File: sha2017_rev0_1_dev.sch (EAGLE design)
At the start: 82 parts, among them IC1 CP210X_USB_UART, IC2 AP7215, IC32 ESP32_AI, Q1 MMBT2222A, Q2 MMBT2222A, Q6 MOSFET-NCHANNELBSS123LT1G, SW801 MCMT5-F-V, X701 2908-05WB-MG

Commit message: fixed all part designators
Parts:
- removed C26: 4u7/16V, rcl:C-EUC0805
- removed C27: 2u2/16V, rcl:C-EUC0805
- removed D10, D11: NSVR0320MW2T1G, SparkFun-DiscreteSemi:BAT20JFILM
- removed SJ14: JUMPER-PAD-2-NC_BY_TRACE, SparkFun-Passives:JUMPER-PAD-2-NC_BY_TRACE
- added C8: 100n, rcl:C-EUC0805
- added C9: 1u, rcl:C-EUC0603
- added D100, D6: (no value), SparkFun-LED:LED0603
- added SJ1: JUMPER-PAD-2-NC_BY_TRACE, SparkFun-Passives:JUMPER-PAD-2-NC_BY_TRACE
- C1: value 100n -> 4u7/16V; device rcl:C-EUC0603 -> 00ralf:C0603-DASHES
- C10, C13: value 4u7/16V -> 1u; device 00ralf:C0603-DASHES -> rcl:C-EUC0603
- C11: device rcl:C-EUC0805 -> rcl:C-EUC0603
- C12: value 4u7/16V -> 1u; device rcl:C-EUC0805 -> rcl:C-EUC0603
- C14, C7: value 100n -> 1u
- C15: value 4u7/16V -> 100n; device rcl:C-EUC0805 -> rcl:C-EUC0603
- C19: device rcl:C-EUC0603 -> 00ralf:C0603-DASHES
- C2: value 100n -> 2u2/16V; device rcl:C-EUC0603 -> rcl:C-EUC0805
- C20: value 1u -> 100n
- C21, C22: value 1u -> 4u7/16V; device rcl:C-EUC0603 -> rcl:C-EUC0805
- C23, C24: value 1u -> (none); OC_FARNELL (none) -> unknown
- C25: value 1u -> 100n; device 00ralf:C0603-DASHES -> rcl:C-EUC0603
- C3: value (none) -> 100n; device rcl:C-EUC0603 -> rcl:C-EUC0805; OC_FARNELL unknown -> (none)
- C4: value (none) -> 4u7/16V; device rcl:C-EUC0603 -> rcl:C-EUC0805; OC_FARNELL unknown -> (none)
- C5: value 100n -> 4u7/16V; device rcl:C-EUC0805 -> 00ralf:C0603-DASHES
- D1: value (none) -> PMEG4005EJ; device SparkFun-LED:LED0603 -> SparkFun-DiscreteSemi:DIODE-SCHOTTKY-PMEG4005EJ
- D2: value (none) -> NSVR0320MW2T1G; device SparkFun-LED:LED0603 -> SparkFun-DiscreteSemi:BAT20JFILM
- D3: value PMEG4005EJ -> NSVR0320MW2T1G; device SparkFun-DiscreteSemi:DIODE-SCHOTTKY-PMEG4005EJ -> SparkFun-DiscreteSemi:BAT20JFILM
- IC1: value CP210X_USB_UART -> AP7215; device SparkFun-DigitalIC:CP210X_USB_UART -> badge:AP7215
- IC2: value AP7215 -> (none); device badge:AP7215 -> SparkFun-PowerIC:V_REG_LM1117SOT223
- IC3: value (none) -> CP210X_USB_UART; device SparkFun-PowerIC:V_REG_LM1117SOT223 -> SparkFun-DigitalIC:CP210X_USB_UART
- JP2: value M11LOCK -> M09LOCK; device SparkFun-Connectors:M11LOCK -> SparkFun-Connectors:M09LOCK
- JP3: value M09LOCK -> M11LOCK; device SparkFun-Connectors:M09LOCK -> SparkFun-Connectors:M11LOCK
- R1, R2: value 10K -> (none)
- R11: value 10k -> (none)
- R14, R15, R16, R17: value (none) -> 10k
- R4: value 10k -> (none); OC_FARNELL unknown -> (none)
- R5, R6: value 10k -> 10K
- R7: value 10k -> 5R; device rcl:R-EU_R0603 -> 00ralf:R0603-DASHES
- R8: OC_FARNELL (none) -> unknown
- R9: value 5R -> 10k; device 00ralf:R0603-DASHES -> rcl:R-EU_R0603
- renumbered IC32 to IC4, J2 to J1, Q6 to Q3, R714 to R10, S5 to S101, S6 to S100, SW801 to SW100, USB100 to USB1
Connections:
- net +3V3: now also C19.1, C20.1, C21.1, C22.1, C4.1, C5.1, IC1.OUT, IC2.OUT@1, JP1.11, R15.2, R16.2, R17.2, R8.1, R9.2; no longer C12.1, C13.1, C14.1, C26.1, C6.1, C7.1, IC3.OUT, IC3.OUT@1, JP2.11, R4.1, R5.2, R6.2, R7.2, R8.2
- net +5V: now also C2.1, C3.1, C8.1, D1.C, IC1.IN, IC3.REGIN, IC3.VBUS; no longer C10.1, C27.1, C5.1, D3.C, IC1.REGIN, IC1.VBUS, IC3.IN
- net BT_B: now also R17.1, SJ13.1; no longer R12.1, SJ7.1
- net BT_DOWN: now also R13.1, SJ9.1; no longer R6.1, SJ3.1
- net BT_LEFT: now also R14.1, SJ10.1; no longer R7.1, SJ4.1
- net BT_MID: now also R15.1, SJ11.1; no longer R11.1, SJ6.1
- net BT_RIGHT: now also R12.1, SJ8.1; no longer R8.1, SJ2.1
- net BT_UP: now also R16.1, SJ12.1; no longer R5.1, SJ5.1
- net ESP32_!RESET: now also JP3.10, R8.2; no longer JP1.10, R4.2
- net ESP32_FLASH/TOUCHE_MENU: now also JP2.3, R9.1; no longer JP3.3, R13.1
- net ESP32_RX: now also D4.C, IC3.TXD, JP1.4; no longer D2.C, IC1.TXD, JP2.4
- net ESP32_TX: now also D6.C, IC3.RXD, JP1.3; no longer D4.C, IC1.RXD, JP2.3
- net GND: now also C10.1, C12.1, C13.1, C19.2, C20.2, C21.2, C22.2, C3.2, C4.2, C7.1, C8.2, C9.1, D1.A, D3.C, IC2.ADJ, IC3.GND, IC3.GND@EXP, IC3.GND@M, JP1.1, JP2.5, JP3.11, R7.2; no longer C10.2, C12.2, C13.2, C14.2, C20.1, C21.1, C22.1, C26.2, C27.2, C3.1, C4.1, C7.2, D11.C, D3.A, IC1.GND@EXP, IC1.GND@M, IC2.GND, IC3.ADJ, JP1.11, JP2.1, JP3.5, R9.2
- net LCD_!RESET: now also SJ3.2; no longer SJ8.2
- net LCD_BUSY: now also SJ2.2; no longer SJ12.2
- net LCD_CS: now also SJ5.2; no longer SJ9.2
- net LCD_D/!S: now also SJ4.2; no longer SJ14.2
- net LCD_MOSI: now also SJ7.2; no longer SJ11.2
- net LCD_SCK: now also SJ6.2; no longer SJ10.2
- net LED1: now also D100.C, SJ1.2; no longer D1.C, SJ13.2
- net N$1: now also C23.2, JP3.9; no longer C3.2, JP1.9
- net N$10: now also IC3.RTS, R5.1; no longer IC1.RTS, R2.1
- net N$11: now also IC3.DTR, R6.1; no longer IC1.DTR, R1.1
- net N$12: now also JP3.6, SJ8.2; no longer JP1.6, SJ2.2
- net N$13: now also R5.2; no longer R2.2
- net N$14: now also R6.2; no longer R1.2
- net N$15: now also JP3.7; no longer JP1.7
- net N$16: now also JP1.2, SJ1.1; no longer JP2.2, SJ13.1
- net N$17: now also JP1.5, SJ2.1; no longer JP2.5, SJ12.1
- net N$18: now also JP1.7, SJ4.1; no longer JP2.7, SJ14.1
- net N$19: now also JP1.6, SJ3.1; no longer JP2.6, SJ8.1
- net N$2: now also C24.2, JP3.8; no longer C4.2, JP1.8
- net N$20: now also JP1.8, SJ5.1; no longer JP2.8, SJ9.1
- net N$21: now also JP1.9, SJ6.1; no longer JP2.9, SJ10.1
- net N$22: now also C14.1, D2.C, D3.A; no longer C19.1, D10.C, D11.A
- net N$23: now also C14.2; no longer C19.2
- net N$24: now also JP1.10, SJ7.1; no longer JP2.10, SJ11.1
- net N$25: now also D100.A, R11.1; no longer D1.A, R14.1
- net N$26: now also R2.1; no longer R15.1
- net N$27: now also D4.A, R1.1; no longer D2.A, R16.1
- net N$28: now also D6.A, R4.1; no longer D4.A, R17.1
- net N$3: now also JP3.1, SJ13.2; no longer JP1.1, SJ7.2
- net N$4: now also JP3.2, SJ12.2; no longer JP1.2, SJ5.2
- net N$6: now also JP3.3, SJ11.2; no longer JP1.3, SJ6.2
- net N$7: now also JP3.4, SJ10.2; no longer JP1.4, SJ4.2
- net N$8: now also IC3.!RST; no longer IC1.!RST
- net N$9: now also JP3.5, SJ9.2; no longer JP1.5, SJ3.2
- net PREVGH: now also C13.2; no longer C17.2
- net PREVGL: now also C9.2, D2.A; no longer C18.2, D10.A
- net RESE: now also R7.1; no longer R9.1
- net SD_CD: now also JP2.1; no longer JP3.1
- net SD_CLK: now also JP2.9; no longer JP3.9
- net SD_CMD: now also JP2.6; no longer JP3.6
- net SD_DATA0: now also JP2.4; no longer JP3.4
- net SD_DATA1: now also JP2.2; no longer JP3.2
- net SD_DATA2: now also JP2.8; no longer JP3.8
- net SD_DATA3: now also JP2.7; no longer JP3.7
- net USB_DN_CON: now also IC3.D-; no longer IC1.D-
- net USB_DP_CON: now also IC3.D+; no longer IC1.D+
- net VCOM: now also C7.2; no longer C24.2
- net VDD: now also C6.1, IC3.VDD, R1.2, R2.2, R4.2; no longer C2.1, IC1.VDD, R15.2, R16.2, R17.2
- net VGH: now also C17.2; no longer C21.2
- net VGL: now also C18.2; no longer C20.2
- net VSH: now also C12.2; no longer C22.2
- net VSL: now also C10.2; no longer C23.2

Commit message: some PCB tweeking
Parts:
- added FD1, FD2, FD3, FD4, FD5: FIDUCIAL, adafruit:FIDUCIAL
- D1: value PMEG4005EJ -> SD05-7
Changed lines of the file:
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@@
 <part name="GND46" library="supply1" deviceset="GND" device=""/>
 <part name="F1" library="SparkFun-PowerIC" deviceset="PTC" device="SMD" value="500mA"/>
-<part name="D1" library="SparkFun-DiscreteSemi" deviceset="DIODE-SCHOTTKY" device="-PMEG4005EJ" value="PMEG4005EJ"/>
+<part name="D1" library="SparkFun-DiscreteSemi" deviceset="DIODE-SCHOTTKY" device="-PMEG4005EJ" value="SD05-7"/>
 <part name="GND26" library="supply1" deviceset="GND" device=""/>
 <part name="FRAME1" library="frames" deviceset="A3L-LOC" device=""/>
@@
 <part name="C15" library="rcl" deviceset="C-EU" device="C0603" value="100n"/>
 <part name="GND17" library="supply1" deviceset="GND" device=""/>
+<part name="FD4" library="adafruit" deviceset="FIDUCIAL" device="">
+<attribute name="MF" value=""/>
+<attribute name="MPN" value=""/>
+<attribute name="OC_FARNELL" value="unknown"/>
+</part>
+<part name="FD3" library="adafruit" deviceset="FIDUCIAL" device="">
+<attribute name="MF" value=""/>
+<attribute name="MPN" value=""/>
+<attribute name="OC_FARNELL" value="unknown"/>
+</part>
+<part name="FD1" library="adafruit" deviceset="FIDUCIAL" device="">
+<attribute name="MF" value=""/>
+<attribute name="MPN" value=""/>
+<attribute name="OC_FARNELL" value="unknown"/>
+</part>
+<part name="FD2" library="adafruit" deviceset="FIDUCIAL" device="">
+<attribute name="MF" value=""/>
+<attribute name="MPN" value=""/>
+<attribute name="OC_FARNELL" value="unknown"/>
+</part>
+<part name="FD5" library="adafruit" deviceset="FIDUCIAL" device="">
+<attribute name="MF" value=""/>
+<attribute name="MPN" value=""/>
+<attribute name="OC_FARNELL" value="unknown"/>
+</part>
 </parts>
 <sheets>
@@
 <instance part="C15" gate="G$1" x="165.1" y="71.12"/>
 <instance part="GND17" gate="1" x="165.1" y="63.5"/>
+<instance part="FD4" gate="G$1" x="16.51" y="10.16">
+<attribute name="OC_FARNELL" x="16.51" y="10.16" size="1.778" layer="96" rot="MR0" display="off"/>
+<attribute name="MF" x="16.51" y="10.16" size="1.778" layer="96" rot="MR0" display="off"/>
+<attribute name="MPN" x="16.51" y="10.16" size="1.778" layer="96" rot="MR0" display="off"/>
+</instance>
+<instance part="FD3" gate="G$1" x="25.4" y="10.16">
+<attribute name="OC_FARNELL" x="25.4" y="10.16" size="1.778" layer="96" rot="MR0" display="off"/>
+<attribute name="MF" x="25.4" y="10.16" size="1.778" layer="96" rot="MR0" display="off"/>
+<attribute name="MPN" x="25.4" y="10.16" size="1.778" layer="96" rot="MR0" display="off"/>
+</instance>
+<instance part="FD1" gate="G$1" x="34.29" y="10.16">
+<attribute name="OC_FARNELL" x="34.29" y="10.16" size="1.778" layer="96" rot="MR0" display="off"/>
+<attribute name="MF" x="34.29" y="10.16" size="1.778" layer="96" rot="MR0" display="off"/>
+<attribute name="MPN" x="34.29" y="10.16" size="1.778" layer="96" rot="MR0" display="off"/>
+</instance>
+<instance part="FD2" gate="G$1" x="43.18" y="10.16">
+<attribute name="OC_FARNELL" x="43.18" y="10.16" size="1.778" layer="96" rot="MR0" display="off"/>
+<attribute name="MF" x="43.18" y="10.16" size="1.778" layer="96" rot="MR0" display="off"/>
+<attribute name="MPN" x="43.18" y="10.16" size="1.778" layer="96" rot="MR0" display="off"/>
+</instance>
+<instance part="FD5" gate="G$1" x="50.8" y="10.16">
+<attribute name="OC_FARNELL" x="50.8" y="10.16" size="1.778" layer="96" rot="MR0" display="off"/>
+<attribute name="MF" x="50.8" y="10.16" size="1.778" layer="96" rot="MR0" display="off"/>
+<attribute name="MPN" x="50.8" y="10.16" size="1.778" layer="96" rot="MR0" display="off"/>
+</instance>
 </instances>
 <busses>

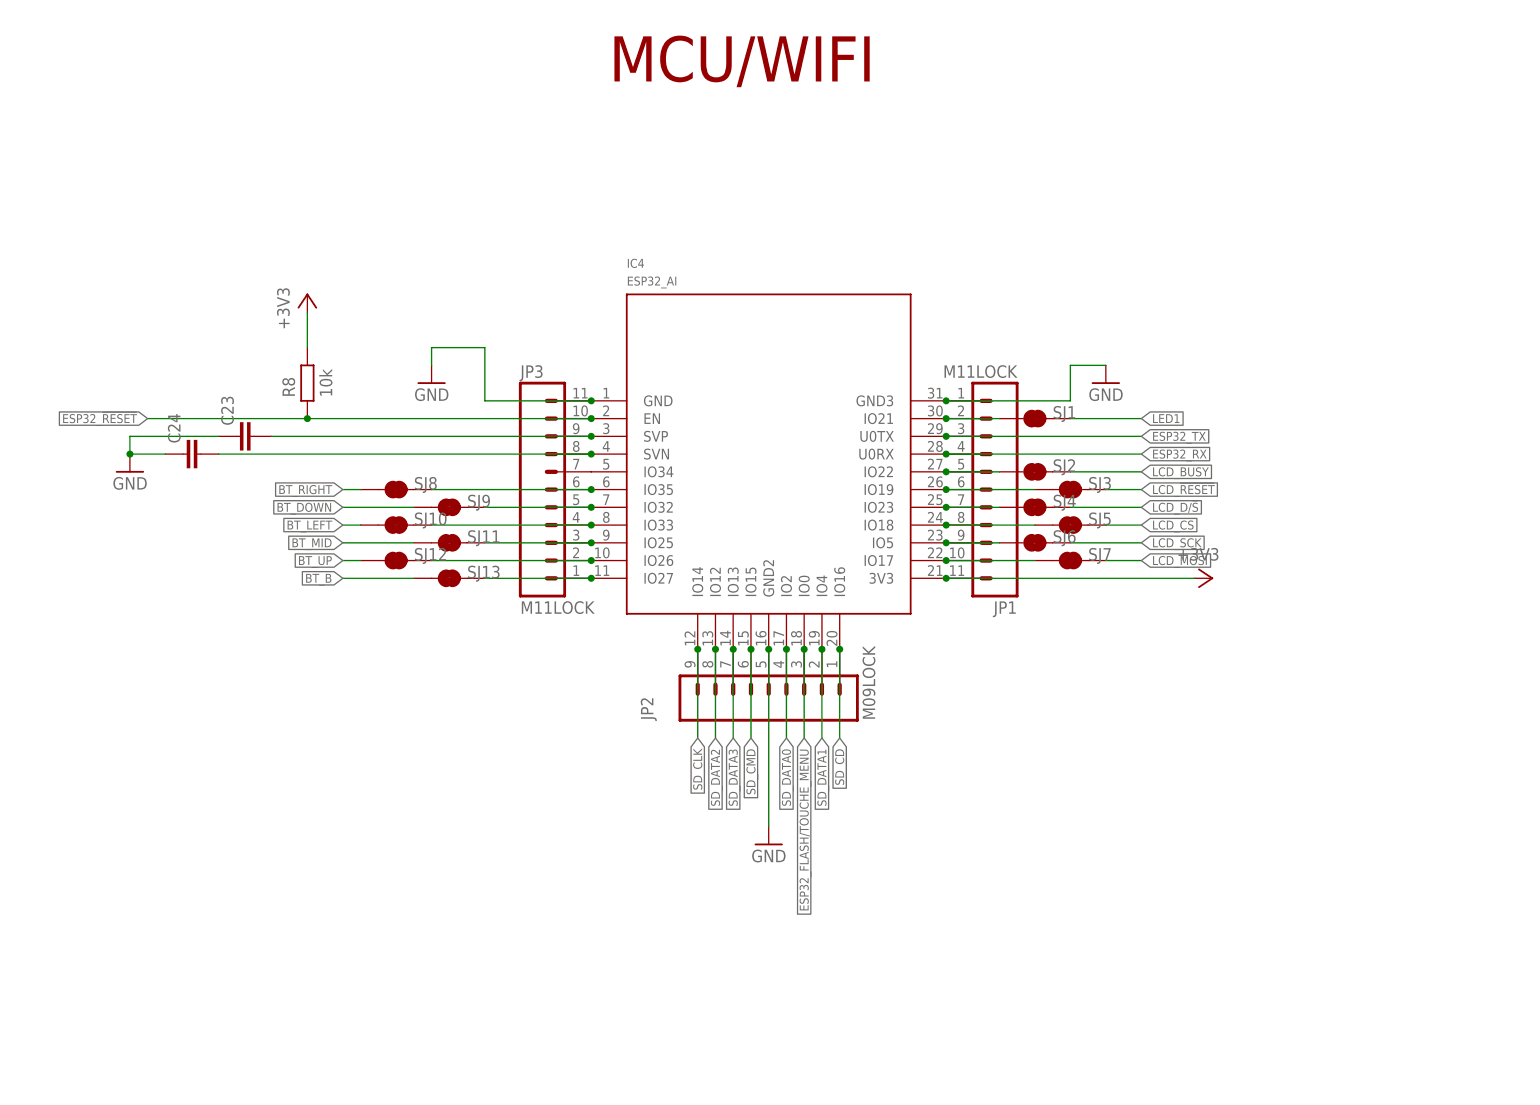
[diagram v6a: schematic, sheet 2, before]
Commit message: changed ESP module to WROOM32
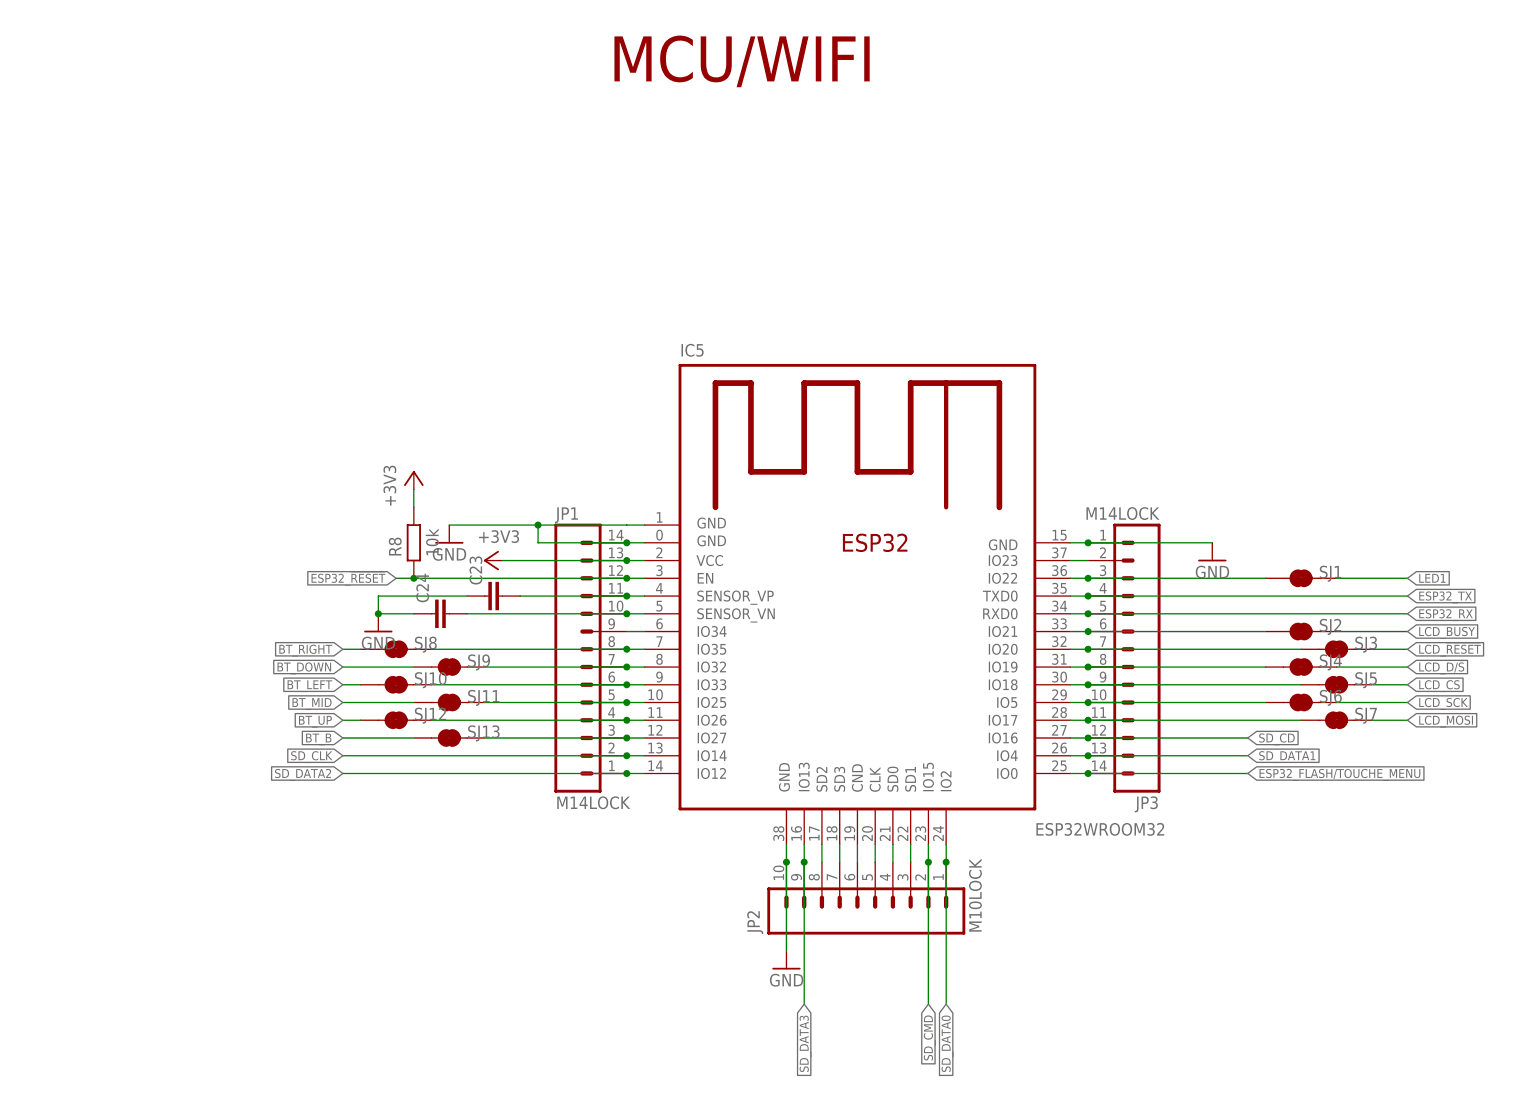
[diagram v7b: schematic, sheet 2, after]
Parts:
- removed IC4: ESP32_AI, badge:ESP32_AI
- added IC5: ESP32WROOM32, ESP3x:ESP32WROOM32
- C1, C5: value 4u7/16V -> 100n; device 00ralf:C0603-DASHES -> rcl:C-EUC0603; PARTNO (none) -> GRM188R71H104KA93D
- C10, C12, C13, C14, C17, C18, C7, C9: PARTNO (none) -> GRM188R61E105KA12D
- C11, C15, C20, C25, C6: PARTNO (none) -> GRM188R71H104KA93D
- C16, C21, C22, C4: PARTNO (none) -> GRM21BR61C475KA88K
- C19: device 00ralf:C0603-DASHES -> rcl:C-EUC0603; PARTNO (none) -> GRM188R61E105KA12D
- C2: value 2u2/16V -> 4u7/16V; PARTNO (none) -> GRM21BR61C475KA88K
- C3, C8: value 100n -> 4u7/16V; PARTNO (none) -> GRM21BR61C475KA88K
- D1: PARTNO (none) -> PMEG4005EJ,115
- D100: value (none) -> Green; device SparkFun-LED:LED0603 -> led:LEDSML1206; PARTNO (none) -> 156120VS75300
- D2, D3, D7: PARTNO (none) -> BAT20JFILM
- D4: value (none) -> Yellow
- D5: value (none) -> green
- D6: value (none) -> RED
- F1: PARTNO (none) -> 0ZCJ0025FF2E
- IC1: PARTNO (none) -> AP7215-33YG-13
- IC2: value (none) -> LM1117; PARTNO (none) -> LM1117MPX-3.3/NOPB
- IC3: PARTNO (none) -> CP2102-GMR
- J1: PARTNO (none) -> 68712414022
- JP1, JP3: value M11LOCK -> M14LOCK; device SparkFun-Connectors:M11LOCK -> SparkFun-Connectors:M14LOCK
- JP2: value M09LOCK -> M10LOCK; device SparkFun-Connectors:M09LOCK -> SparkFun-Connectors:M10LOCK
- L1: PARTNO (none) -> NLCV32T-220K-EF
- Q1, Q2: PARTNO (none) -> BC817-25,215
- Q3: value MOSFET-NCHANNELBSS123LT1G -> SI1304 BDL; device SparkFun-DiscreteSemi:MOSFET-NCHANNELBSS123LT1G -> SparkFun-DiscreteSemi:MOSFET-NCHANNEL2N7002PW; PARTNO (none) -> SI1308EDL-T1-GE3
- R1, R11, R2, R4: value (none) -> 1k; PARTNO (none) -> ERJ-3GEYJ102V
- R10: PARTNO (none) -> CRCW0603100KFKEA
- R12, R13, R14, R15, R16, R17, R8, R9: PARTNO (none) -> ERJ-3GEYJ103V
- R3: device 00ralf:R0603-DASHES -> rcl:R-EU_R0603; PARTNO (none) -> ERJ-3GEYJ103V
- R5, R6: value 10K -> 10k; PARTNO (none) -> ERJ-3GEYJ103V
- R7: PARTNO (none) -> ERJ-3GEYJ5R1V
- S1, S100, S101: PARTNO (none) -> SKHMQME010
- SW100: PARTNO (none) -> SKRHAAE010
- USB1: PARTNO (none) -> 10118194-0001LF
- X701: PARTNO (none) -> 2908-05WB-MG
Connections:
- removed net N$19: IC4.IO19, JP1.6, SJ3.1
- removed net N$2: C24.2, IC4.SVN, JP3.8
- new net N$42: C23.2, IC5.SENSOR_VP, JP1.11
- new net N$43: C24.2, IC5.SENSOR_VN, JP1.10
- new net N$44: IC5.IO35, JP1.8, SJ8.2
- new net N$45: IC5.IO32, JP1.7, SJ9.2
- new net N$46: IC5.IO33, JP1.6, SJ10.2
- new net N$47: IC5.IO25, JP1.5, SJ11.2
- new net N$48: IC5.IO26, JP1.4, SJ12.2
- new net N$49: IC5.IO27, JP1.3, SJ13.2
- new net N$63: IC5.IO19, JP3.8, SJ4.1
- net +3V3: now also IC5.VCC, JP1.13; no longer IC4.3V3, JP1.11
- net ESP32_!RESET: now also IC5.EN, JP1.12; no longer IC4.EN, JP3.10
- net ESP32_FLASH/TOUCHE_MENU: now also IC5.IO0, JP3.14; no longer IC4.IO0, JP2.3
- net ESP32_RX: now also IC5.RXD0, JP3.5; no longer IC4.U0RX, JP1.4
- net ESP32_TX: now also IC5.TXD0, JP3.4; no longer IC4.U0TX, JP1.3
- net GND: now also IC5.GND, IC5.GND@0, IC5.GND@1, IC5.GND@3, JP1.14, JP2.10, JP3.1; no longer IC4.GND, IC4.GND2, IC4.GND3, JP1.1, JP2.5, JP3.11
- net N$1: now also IC5.IO34, JP1.9; no longer C23.2, IC4.SVP, JP3.9
- net N$12: now also IC5.SD1, JP2.3; no longer IC4.IO35, JP3.6, SJ8.2
- net N$15: now also IC5.IO23, JP3.2; no longer IC4.IO34, JP3.7
- net N$16: now also IC5.IO22, JP3.3; no longer IC4.IO21, JP1.2
- net N$17: now also IC5.IO21, JP3.6; no longer IC4.IO22, JP1.5
- net N$18: now also IC5.IO20, JP3.7, SJ3.1; no longer IC4.IO23, JP1.7, SJ4.1
- net N$20: now also IC5.IO18, JP3.9; no longer IC4.IO18, JP1.8
- net N$21: now also IC5.IO5, JP3.10; no longer IC4.IO5, JP1.9
- net N$24: now also IC5.IO17, JP3.11; no longer IC4.IO17, JP1.10
- net N$3: now also IC5.SD2, JP2.8; no longer IC4.IO27, JP3.1, SJ13.2
- net N$4: now also IC5.SD3, JP2.7; no longer IC4.IO26, JP3.2, SJ12.2
- net N$6: now also IC5.CND, JP2.6; no longer IC4.IO25, JP3.3, SJ11.2
- net N$7: now also IC5.CLK, JP2.5; no longer IC4.IO33, JP3.4, SJ10.2
- net N$9: now also IC5.SD0, JP2.4; no longer IC4.IO32, JP3.5, SJ9.2
- net SD_CD: now also IC5.IO16, JP3.12; no longer IC4.IO16, JP2.1
- net SD_CLK: now also IC5.IO14, JP1.2; no longer IC4.IO14, JP2.9
- net SD_CMD: now also IC5.IO15, JP2.2; no longer IC4.IO15, JP2.6
- net SD_DATA0: now also IC5.IO2, JP2.1; no longer IC4.IO2, JP2.4
- net SD_DATA1: now also IC5.IO4, JP3.13; no longer IC4.IO4, JP2.2
- net SD_DATA2: now also IC5.IO12, JP1.1; no longer IC4.IO12, JP2.8
- net SD_DATA3: now also IC5.IO13, JP2.9; no longer IC4.IO13, JP2.7
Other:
- moved on the sheet: C19, C23, C24, R8, SJ1, SJ10, SJ11, SJ12, SJ13, SJ2, SJ3, SJ4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
